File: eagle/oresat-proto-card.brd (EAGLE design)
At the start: 99 x 95.3 mm, 107 parts, among them J1 J-SAMTEC-TFM-110-X1-XXX-D-RA, J2 U.FL, J3 U.FL, J4 U.FL, J6 J-SAMTEC-TFM-120-X1-XXX-D-RA, J7 FTSH-105-XX-X-DV-K, Q3 MOSFET-PCH-SOT23-6, Q4 MOSFET-PCH-SOT23-6, Q5 PMV45EN, Q6 PMV45EN, U2 TCAN330, U3 MAX7310ATE, U4 MAX4211CETE, U5 TPS62111RSA, U6 STM32F042K6, U7 MCP1703A, X1 16MHZ-2.5x2mm

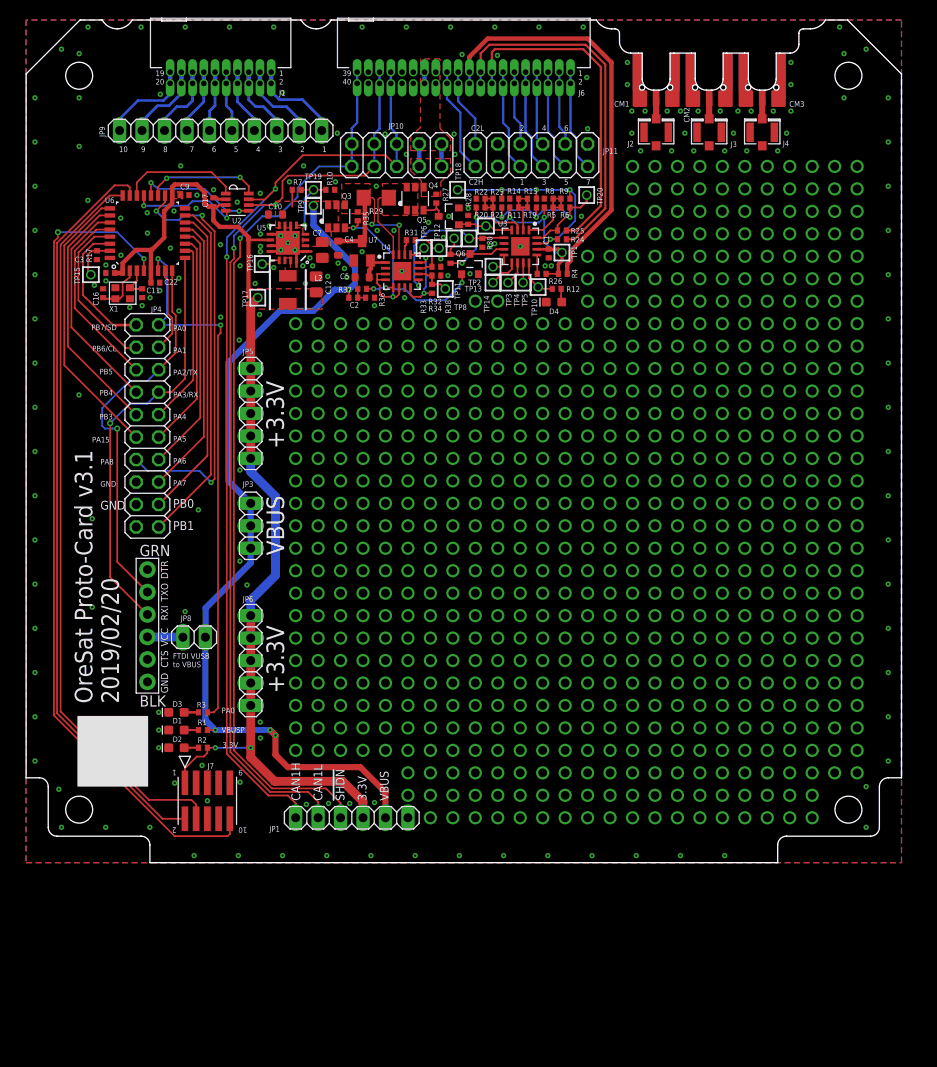
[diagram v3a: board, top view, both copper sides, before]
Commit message: Added new safety circuit on the I2C of the OPD.
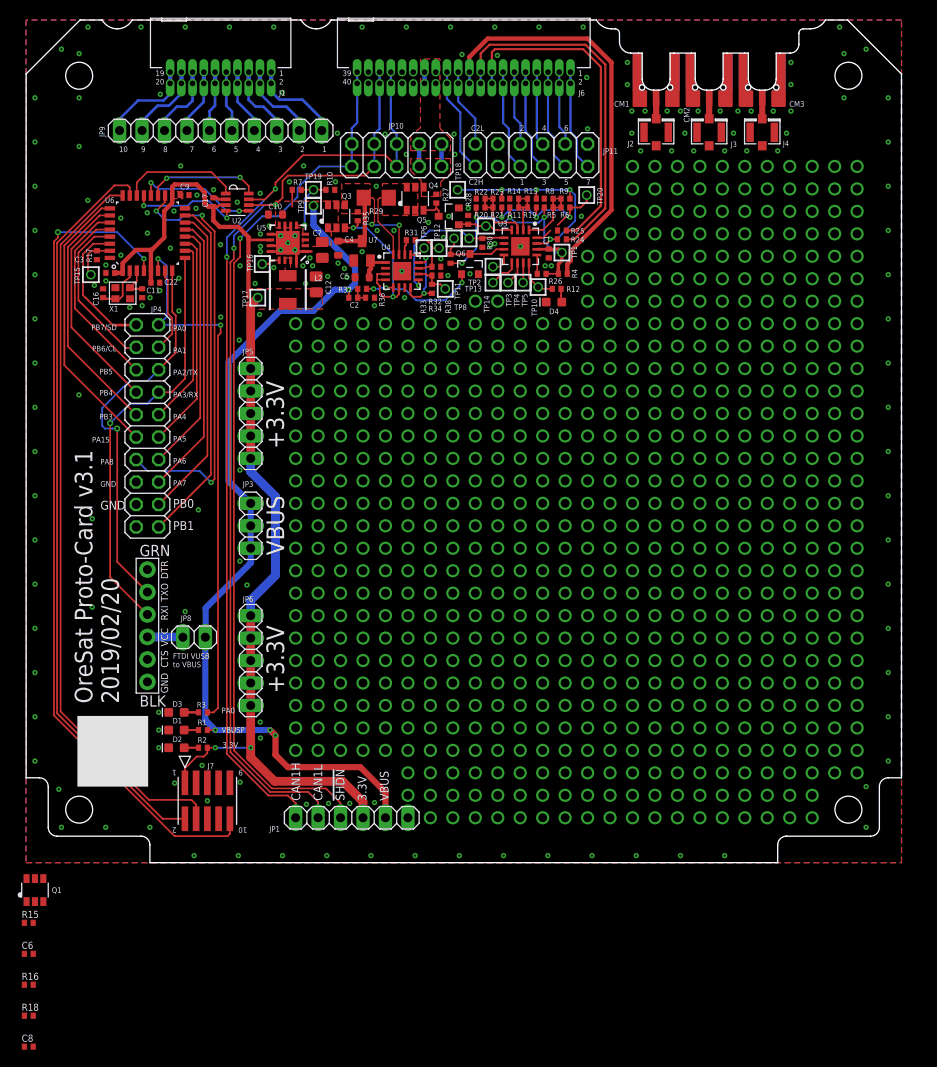
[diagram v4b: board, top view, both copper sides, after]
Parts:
- added C6, C8: TBD, rcl_custom:.0402-B-NOSILK
- added Q1: DMP2240UDM, Q-MOSFET-PCH-dual-SOT23-6:SOT23-6
- added R15, R16, R18: 10k, rcl_custom:.0402-B-NOSILK
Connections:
- new net N$579: C6.1, Q1.5, R25.2
- new net N$580: C6.2, Q1.1, Q1.4, R15.2
- new net N$581: C8.2, Q1.3, R16.2, R18.1
- net GND: now also R15.1
- net PEN-SDA-FILT: now also Q1.6, R16.1; no longer R25.2
- net VPD: now also C8.1, Q1.2, R18.2
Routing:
- net PEN-SDA-FILT: track 20.3 -> 18.9 mm
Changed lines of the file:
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@@
 <setting verticaltext="up"/>
 </settings>
-<grid distance="0.1" unitdist="mm" unit="mm" style="lines" multiple="1" display="yes" altdistance="0.025" altunitdist="inch" altunit="inch"/>
+<grid distance="0.01" unitdist="mm" unit="mm" style="lines" multiple="1" display="yes" altdistance="0.025" altunitdist="inch" altunit="inch"/>
 <layers>
 <layer number="1" name="Top" color="4" fill="1" visible="yes" active="yes"/>
@@
 <attribute name="VALUE" x="60.8" y="66.25" size="0.8" layer="27" font="vector" ratio="15" rot="R180"/>
 </element>
+<element name="Q1" library="Q-MOSFET-PCH-dual-SOT23-6" package="SOT23-6" value="DMP2240UDM" x="1" y="-3.1" smashed="yes">
+<attribute name="MFR" value="Diodes Inc" x="1" y="-3.1" size="1.778" layer="27" display="off"/>
+<attribute name="MPN" value="DMP2240UDM" x="1" y="-3.1" size="1.778" layer="27" display="off"/>
+<attribute name="NAME" x="2.902" y="-3.417" size="0.635" layer="25" font="vector" ratio="20"/>
+</element>
+<element name="R15" library="rcl_custom" package=".0402-B-NOSILK" value="10k" x="0.3" y="-6.8" smashed="yes">
+<attribute name="DIS" value="Digi-Key" x="0.3" y="-6.8" size="0.635" layer="27" ratio="20" display="off"/>
+<attribute name="DPN" value="1276-4275-1-ND" x="0.3" y="-6.8" size="0.635" layer="27" ratio="20" display="off"/>
+<attribute name="MFR" value="Samsung" x="0.3" y="-6.8" size="0.635" layer="27" ratio="20" display="off"/>
+<attribute name="MPN" value="RC1005F6653CS" x="0.3" y="-6.8" size="0.635" layer="27" ratio="20" display="off"/>
+<attribute name="NAME" x="0.3" y="-6.8" size="0.2" layer="33" ratio="15" align="center"/>
+<attribute name="NAME" x="-0.5" y="-6.25" size="0.8" layer="25" font="vector" ratio="15"/>
+<attribute name="VALUE" x="-0.5" y="-8.15" size="0.8" layer="27" font="vector" ratio="15"/>
+</element>
+<element name="C6" library="rcl_custom" package=".0402-B-NOSILK" value="TBD" x="0.3" y="-10.3" smashed="yes">
+<attribute name="DIS" value="Digi-Key" x="0.3" y="-10.3" size="0.635" layer="27" ratio="20" display="off"/>
+<attribute name="DPN" value="1276-1001-1-ND" x="0.3" y="-10.3" size="0.635" layer="27" ratio="20" display="off"/>
+<attribute name="MFR" value="Samsung" x="0.3" y="-10.3" size="0.635" layer="27" ratio="20" display="off"/>
+<attribute name="MPN" value="CL05B104KO5NNNC" x="0.3" y="-10.3" size="0.635" layer="27" ratio="20" display="off"/>
+<attribute name="NAME" x="0.3" y="-10.3" size="0.2" layer="33" ratio="15" align="center"/>
+<attribute name="NAME" x="-0.5" y="-9.75" size="0.8" layer="25" font="vector" ratio="15"/>
+<attribute name="VALUE" x="-0.5" y="-11.65" size="0.8" layer="27" font="vector" ratio="15"/>
+</element>
+<element name="R16" library="rcl_custom" package=".0402-B-NOSILK" value="10k" x="0.3" y="-13.8" smashed="yes">
+<attribute name="DIS" value="Digi-Key" x="0.3" y="-13.8" size="0.635" layer="27" ratio="20" display="off"/>
+<attribute name="DPN" value="1276-4275-1-ND" x="0.3" y="-13.8" size="0.635" layer="27" ratio="20" display="off"/>
+<attribute name="MFR" value="Samsung" x="0.3" y="-13.8" size="0.635" layer="27" ratio="20" display="off"/>
+<attribute name="MPN" value="RC1005F6653CS" x="0.3" y="-13.8" size="0.635" layer="27" ratio="20" display="off"/>
+<attribute name="NAME" x="0.3" y="-13.8" size="0.2" layer="33" ratio="15" align="center"/>
+<attribute name="NAME" x="-0.5" y="-13.25" size="0.8" layer="25" font="vector" ratio="15"/>
+<attribute name="VALUE" x="-0.5" y="-15.15" size="0.8" layer="27" font="vector" ratio="15"/>
+</element>
+<element name="R18" library="rcl_custom" package=".0402-B-NOSILK" value="10k" x="0.3" y="-17.3" smashed="yes">
+<attribute name="DIS" value="Digi-Key" x="0.3" y="-17.3" size="0.635" layer="27" ratio="20" display="off"/>
+<attribute name="DPN" value="1276-4275-1-ND" x="0.3" y="-17.3" size="0.635" layer="27" ratio="20" display="off"/>
+<attribute name="MFR" value="Samsung" x="0.3" y="-17.3" size="0.635" layer="27" ratio="20" display="off"/>
+<attribute name="MPN" value="RC1005F6653CS" x="0.3" y="-17.3" size="0.635" layer="27" ratio="20" display="off"/>
+<attribute name="NAME" x="0.3" y="-17.3" size="0.2" layer="33" ratio="15" align="center"/>
+<attribute name="NAME" x="-0.5" y="-16.75" size="0.8" layer="25" font="vector" ratio="15"/>
+<attribute name="VALUE" x="-0.5" y="-18.65" size="0.8" layer="27" font="vector" ratio="15"/>
+</element>
+<element name="C8" library="rcl_custom" package=".0402-B-NOSILK" value="TBD" x="0.3" y="-20.8" smashed="yes">
+<attribute name="DIS" value="Digi-Key" x="0.3" y="-20.8" size="0.635" layer="27" ratio="20" display="off"/>
+<attribute name="DPN" value="1276-1001-1-ND" x="0.3" y="-20.8" size="0.635" layer="27" ratio="20" display="off"/>
+<attribute name="MFR" value="Samsung" x="0.3" y="-20.8" size="0.635" layer="27" ratio="20" display="off"/>
+<attribute name="MPN" value="CL05B104KO5NNNC" x="0.3" y="-20.8" size="0.635" layer="27" ratio="20" display="off"/>
+<attribute name="NAME" x="0.3" y="-20.8" size="0.2" layer="33" ratio="15" align="center"/>
+<attribute name="NAME" x="-0.5" y="-20.25" size="0.8" layer="25" font="vector" ratio="15"/>
+<attribute name="VALUE" x="-0.5" y="-22.15" size="0.8" layer="27" font="vector" ratio="15"/>
+</element>
 </elements>
 <signals>
@@
 <via x="53.34" y="63.5" extent="1-16" drill="1" shape="octagon"/>
 <contactref element="D4" pad="C"/>
+<contactref element="R15" pad="1"/>
+<wire x1="4" y1="4" x2="-0.2" y2="-6.8" width="0" layer="19" extent="1-1"/>
 </signal>
 <signal name="SWDIO">
@@
 <signal name="PEN-SDA-FILT">
 <contactref element="U3" pad="16"/>
-<contactref element="R25" pad="2"/>
 <contactref element="R9" pad="2"/>
 <contactref element="R19" pad="2"/>
@@
 <wire x1="57.7596" y1="70.675" x2="58.475" y2="70.675" width="0.2" layer="1"/>
 <wire x1="58.475" y1="70.675" x2="59.3" y2="71.5" width="0.2" layer="1"/>
-<wire x1="59.3" y1="71.5" x2="60.1" y2="71.5" width="0.2" layer="1"/>
 <wire x1="61.5" y1="74.1" x2="61.5" y2="73" width="0.2" layer="1"/>
 <via x="61.5" y="73" extent="1-16" drill="0.254"/>
@@
 <wire x1="62.7" y1="74.1" x2="63.4" y2="74.8" width="0.2" layer="1"/>
 <wire x1="63.4" y1="74.8" x2="63.4" y2="75.5" width="0.2" layer="1"/>
-<wire x1="60.1" y1="72.1" x2="60.1" y2="71.5" width="0.2" layer="1"/>
+<contactref element="Q1" pad="6"/>
+<contactref element="R16" pad="1"/>
+<wire x1="60.1" y1="72.1" x2="59.3" y2="71.5" width="0" layer="19" extent="1-1"/>
+<wire x1="0.05" y1="-1.8" x2="53.8" y2="73" width="0" layer="19" extent="1-16"/>
+<wire x1="-0.2" y1="-13.8" x2="0.05" y2="-1.8" width="0" layer="19" extent="1-1"/>
 </signal>
 <signal name="N$589">
@@
 <wire x1="49.3" y1="67.8" x2="50.90485" y2="69.40485" width="0.2" layer="16"/>
 <wire x1="50.90485" y1="69.40485" x2="50.90485" y2="70.93338125" width="0.2" layer="16"/>
+<contactref element="Q1" pad="2"/>
+<contactref element="R18" pad="2"/>
+<contactref element="C8" pad="1"/>
+<wire x1="1" y1="-4.4" x2="48" y2="67.8" width="0" layer="19" extent="1-1"/>
+<wire x1="0.8" y1="-17.3" x2="1" y2="-4.4" width="0" layer="19" extent="1-1"/>
+<wire x1="-0.2" y1="-20.8" x2="0.8" y2="-17.3" width="0" layer="19" extent="1-1"/>
 </signal>
 <signal name="N$385">
@@
 <wire x1="60.577" y1="63.4" x2="60.5" y2="64.077" width="0.2" layer="1"/>
 </signal>
+<signal name="N$579">
+<contactref element="R25" pad="2"/>
+<contactref element="Q1" pad="5"/>
+<contactref element="C6" pad="1"/>
+<wire x1="1" y1="-1.8" x2="60.1" y2="71.5" width="0" layer="19" extent="1-1"/>
+<wire x1="-0.2" y1="-10.3" x2="1" y2="-1.8" width="0" layer="19" extent="1-1"/>
+</signal>
+<signal name="N$580">
+<contactref element="Q1" pad="1"/>
+<contactref element="R15" pad="2"/>
+<contactref element="Q1" pad="4"/>
+<contactref element="C6" pad="2"/>
+<wire x1="0.8" y1="-6.8" x2="0.8" y2="-10.3" width="0" layer="19" extent="1-1"/>
+<wire x1="0.05" y1="-4.4" x2="0.8" y2="-6.8" width="0" layer="19" extent="1-1"/>
+<wire x1="1.95" y1="-1.8" x2="0.05" y2="-4.4" width="0" layer="19" extent="1-1"/>
+</signal>
+<signal name="N$581">
+<contactref element="R16" pad="2"/>
+<contactref element="Q1" pad="3"/>
+<contactref element="C8" pad="2"/>
+<contactref element="R18" pad="1"/>
+<wire x1="-0.2" y1="-17.3" x2="0.8" y2="-20.8" width="0" layer="19" extent="1-1"/>
+<wire x1="0.8" y1="-13.8" x2="-0.2" y2="-17.3" width="0" layer="19" extent="1-1"/>
+<wire x1="1.95" y1="-4.4" x2="0.8" y2="-13.8" width="0" layer="19" extent="1-1"/>
+</signal>
 </signals>

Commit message: Latest card outline from Ryan and Catie, and added the first OPD protection circuit revision.
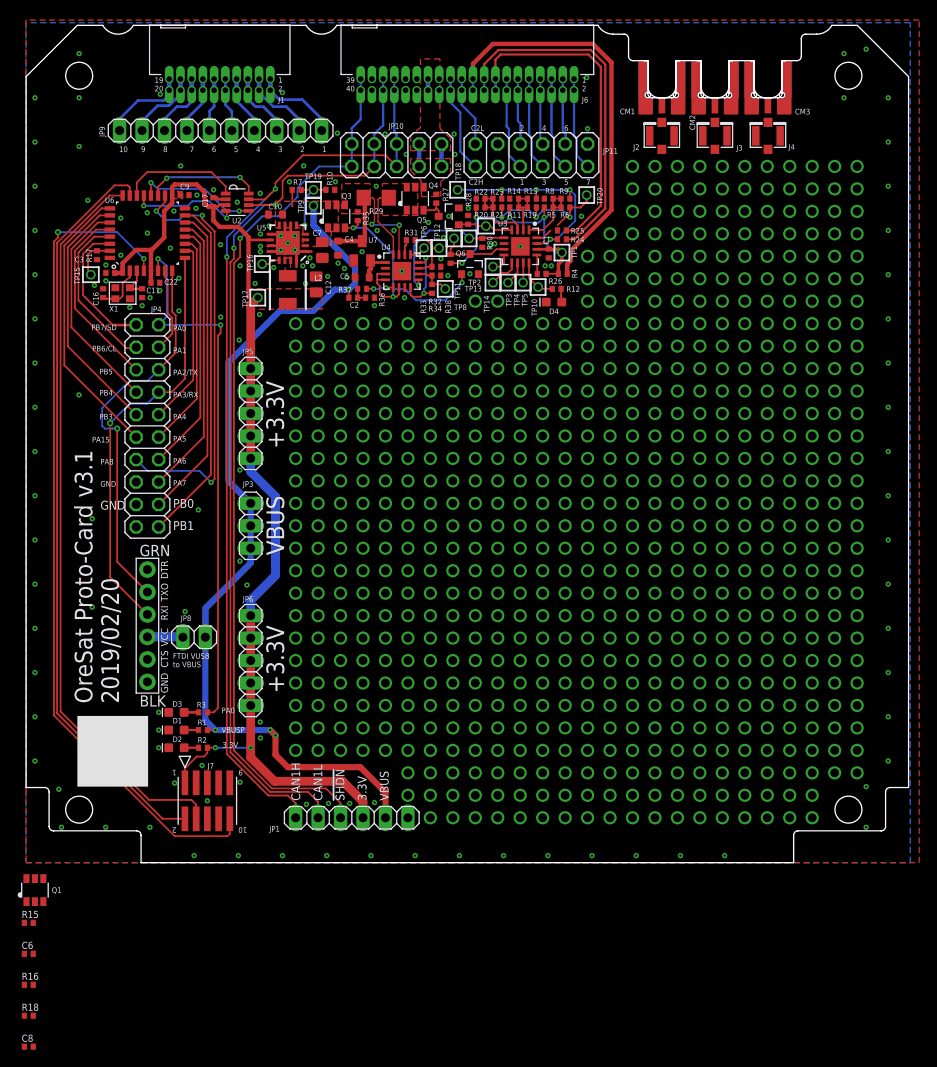
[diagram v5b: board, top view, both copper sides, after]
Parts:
- removed CARD: ORESAT-CARD-V0.5, oresat-card:ORESAT-CARD-V1.0
- added U$1: ORESAT-CARD-V1.1-3XRF, oresat-cards:ORESAT-CARD-V1.1-3XRF
- moved CM1 1.08 mm to (71.9, 90.7)
- moved CM2 1.08 mm to (77.9, 90.7)
- moved CM3 1.08 mm to (83.9, 90.7)
- moved J6 0.87 mm to (49.9, 88.0)
- moved J1 0.78 mm to (21.9, 88.0)
- moved J2 0.76 mm to (71.9, 82.2)
- moved J3 0.76 mm to (77.9, 82.2)
- moved J4 0.76 mm to (83.9, 82.2)
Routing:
- net RF2: track 2.36 -> 0.00 mm
- net RF1: track 2.36 -> 0.00 mm
- net N$300: track 2.36 -> 0.00 mm
- net CAN1_H: track 108.6 -> 107.7 mm
- net SPARE7: track 11.5 -> 10.5 mm
- net SPARE6: track 8.43 -> 7.49 mm
- net SPARE5: track 11.5 -> 10.5 mm
- net SPARE4: track 8.40 -> 7.46 mm
- net SPARE2: track 8.42 -> 7.48 mm
- net SPARE3: track 11.5 -> 10.5 mm
- net SPARE1: track 11.5 -> 10.5 mm
- net CAN2_L: track 12.0 -> 11.1 mm
- net CAN2_H: track 8.93 -> 7.98 mm
- net OPD_SCL: track 40.9 -> 40.1 mm
- net AUX_GND1: track 9.21 -> 8.39 mm
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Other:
- board size 99 x 95.3 mm -> 99.8 x 94.7 mm

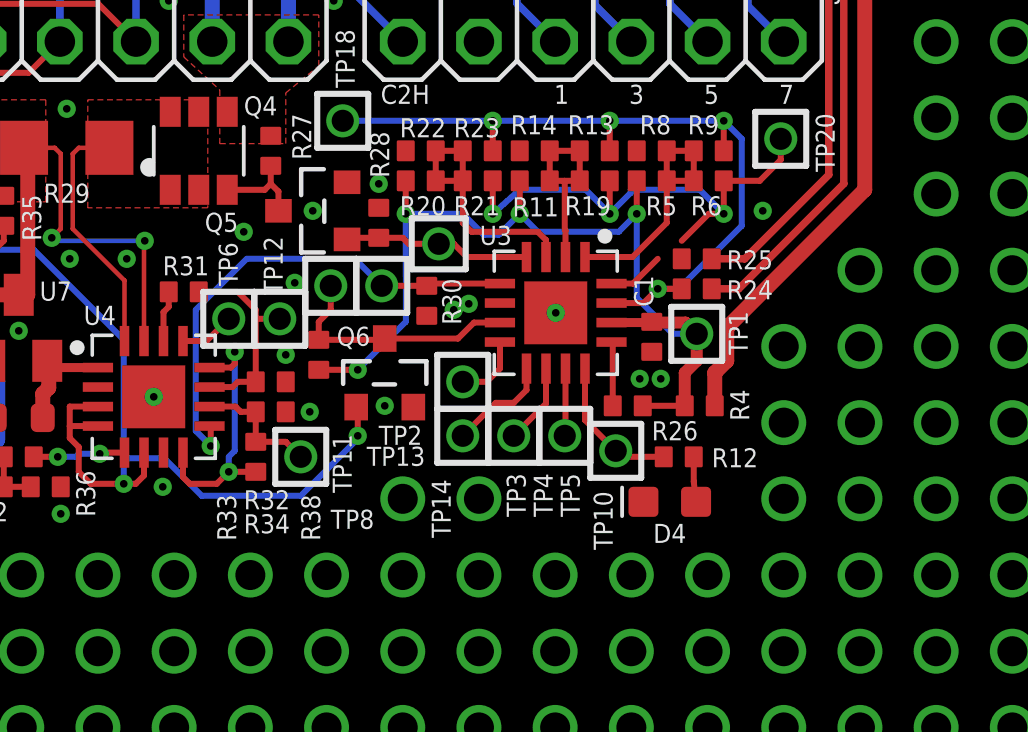
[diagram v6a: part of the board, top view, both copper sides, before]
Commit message: flipped comparator inputs on circuit breaker
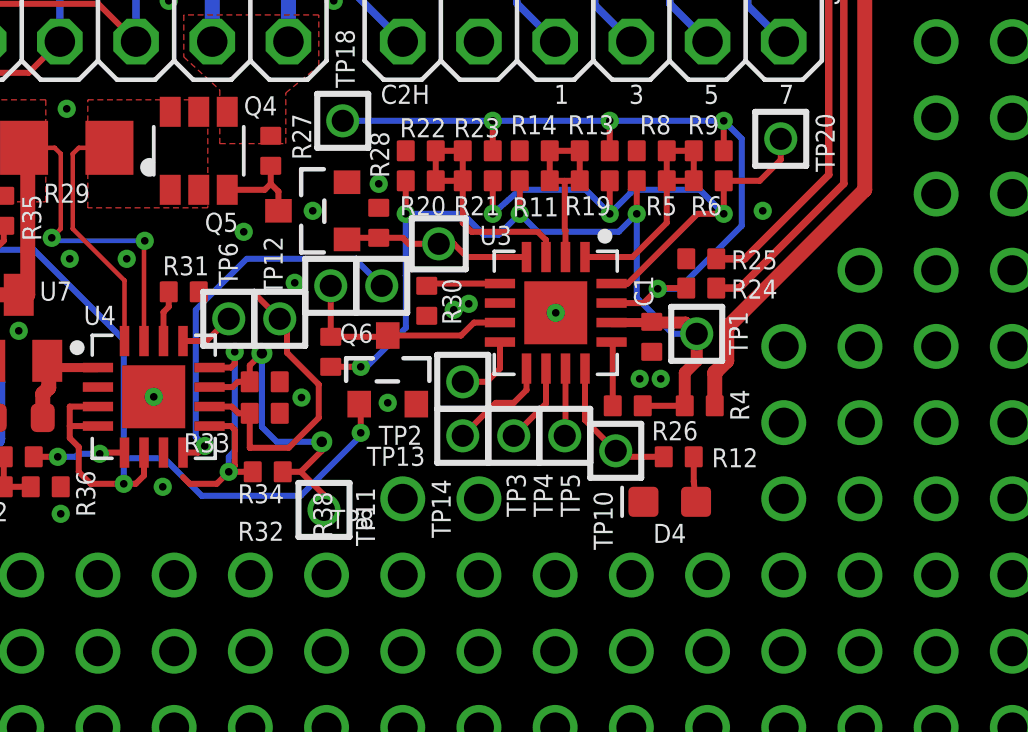
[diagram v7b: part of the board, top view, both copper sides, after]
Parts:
- moved TP11 1.93 mm to (48.2, 63.1)
- moved R32 1.07 mm to (46.2, 66.3)
- moved R34 1.02 mm to (46.2, 67.4)
- moved R33 0.64 mm to (46.3, 64.4), turned to 180 degrees
- moved R38 0.41 mm to (48.4, 68.4)
- moved R24 0.15 mm to (60.8, 70.5)
- moved R25 0.15 mm to (60.8, 71.5)
- moved Q6 0.14 mm to (50.3, 67.8)
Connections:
- net CB-RESET: now also U4.8; no longer U4.9
- net N$596: now also U4.10; no longer U4.11
- net N$597: now also U4.11; no longer U4.10
- net N$599: now also U4.9; no longer U4.8
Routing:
- net N$597: track 4.32 -> 10.7 mm, vias 0 -> 2
- net N$596: track 6.96 -> 12.2 mm
- net CB-RESET: track 16.7 -> 15.1 mm
- net N$599: track 8.87 -> 10.3 mm
- net PEN-SDA-FILT: track 18.9 -> 20.0 mm
- net !FAULT: track 8.24 -> 7.54 mm
- net GND: vias 253 -> 252
